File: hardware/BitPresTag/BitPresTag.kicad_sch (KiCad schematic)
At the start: 28 parts, among them J201 CONN_02X04, J301 Conn_01x01, J302 Conn_01x01, J303 Conn_01x01, J304 Conn_01x01, J401 CONN_01X02, Q501 Q_NPN_BEC, U1 at25ex321D-UUN, U2 AK09940A, U3 LIS2DU12TR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

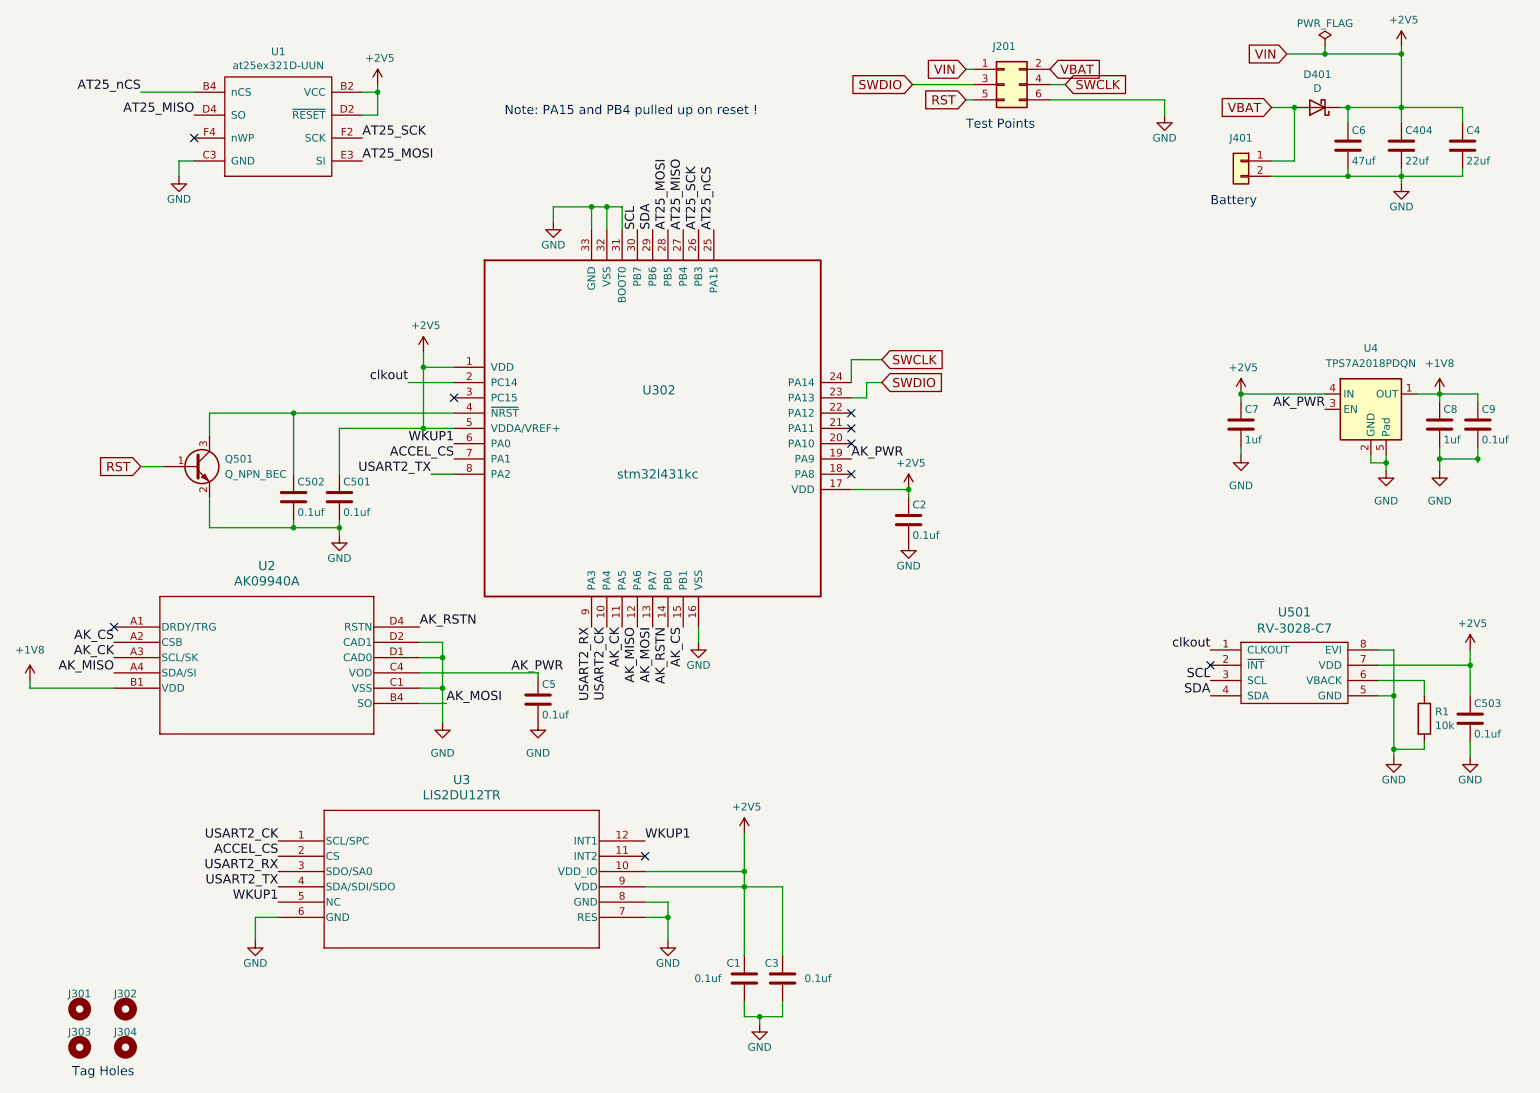
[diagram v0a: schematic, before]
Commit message: added bit/pressure tag design
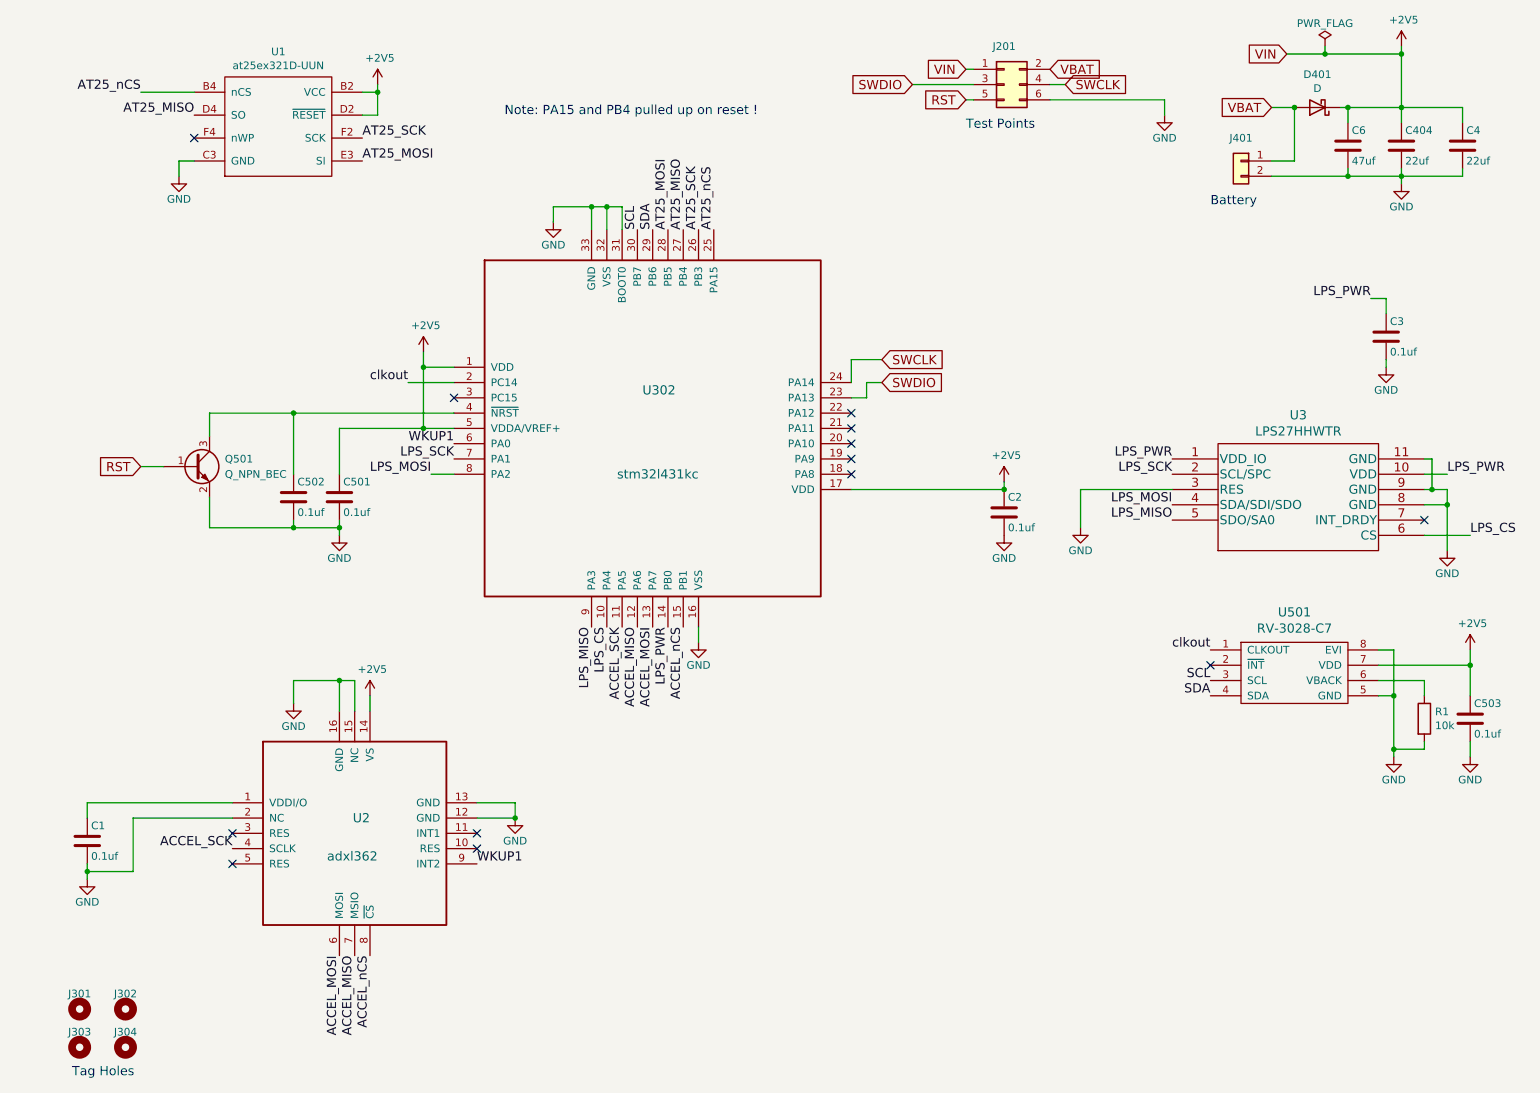
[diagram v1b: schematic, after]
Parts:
- removed C5, C9: 0.1uf, Capacitor_SMD:C_0201_0603Metric, symbol Device:C
- removed C7, C8: 1uf, Capacitor_SMD:C_0201_0603Metric, symbol Device:C
- removed U2: AK09940A, AccelTag:AK09940a, symbol ak09940a:AK09940A
- removed U3: LIS2DU12TR, LGA-12L_LIS2DU12_STM, symbol lis2du12:LIS2DU12TR
- removed U4: TPS7A2018PDQN, Package_SON:Texas_X2SON-4_1x1mm_P0.65mm, symbol Regulator_Linear:TPS7A20xxxDQN
- added U2: adxl362, AccelTag:ADXL362, symbol bittagv7:adxl362
- added U3: LPS27HHWTR, AccelTag:LPS27HHWTR, symbol lps27:LPS27HHWTR
- C1: DISTPN 490-10403-1-ND -> (none); LCSC C181047 -> (none); MFN Murata -> (none); MPN C181047 -> CL05F104ZO5NNNC
- C3: LCSC C181047 -> (none); MPN C181047 -> GRM033C81E104KE14D; Macrofab (none) -> MF-CAP-0402-0.1uF
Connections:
- net +2V5: now also U2.14 (VS); no longer C1.1, C3.1
- net GND: now also U2.12 (GND), U2.13 (GND), U2.15 (NC), U2.16 (GND), U2.2 (NC), U3.11 (GND), U3.3 (RES), U3.8 (GND), U3.9 (GND)
- net WKUP1: now also U2.9 (INT2)
- net ACCEL_CS renamed LPS_SCK
- net LPS_SCK: now also U3.2 (SCL/SPC)
- net AK_CK renamed ACCEL_SCK
- net ACCEL_SCK: now also U2.4 (SCLK)
- net AK_CS renamed ACCEL_nCS
- net ACCEL_nCS: now also U2.8 (~{CS})
- net AK_MISO renamed ACCEL_MISO
- net ACCEL_MISO: now also U2.7 (MSIO)
- net AK_MOSI renamed ACCEL_MOSI
- net ACCEL_MOSI: now also U2.6 (MOSI)
- net AK_PWR: no longer names the net of U302.19 (PA9)
- net AK_RSTN renamed LPS_PWR
- net LPS_PWR: now also C3.1, U3.1 (VDD_IO), U3.10 (VDD)
- net USART2_CK renamed LPS_CS
- net LPS_CS: now also U3.6 (CS)
- net USART2_RX renamed LPS_MISO
- net LPS_MISO: now also U3.5 (SDO/SA0)
- net USART2_TX renamed LPS_MOSI
- net LPS_MOSI: now also U3.4 (SDA/SDI/SDO)
- new net: C1.1, U2.1 (VDDI/O)
- no-connect marks 9 -> 13
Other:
- moved on the sheet: C2
